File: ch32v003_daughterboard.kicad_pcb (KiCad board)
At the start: 2 copper layers, 39 x 45.2 mm, 7 parts, among them J1 Conn_02x05_Odd_Even, J2 Conn_01x03_Pin, P1 Header 7X2, P2 Header 7X2

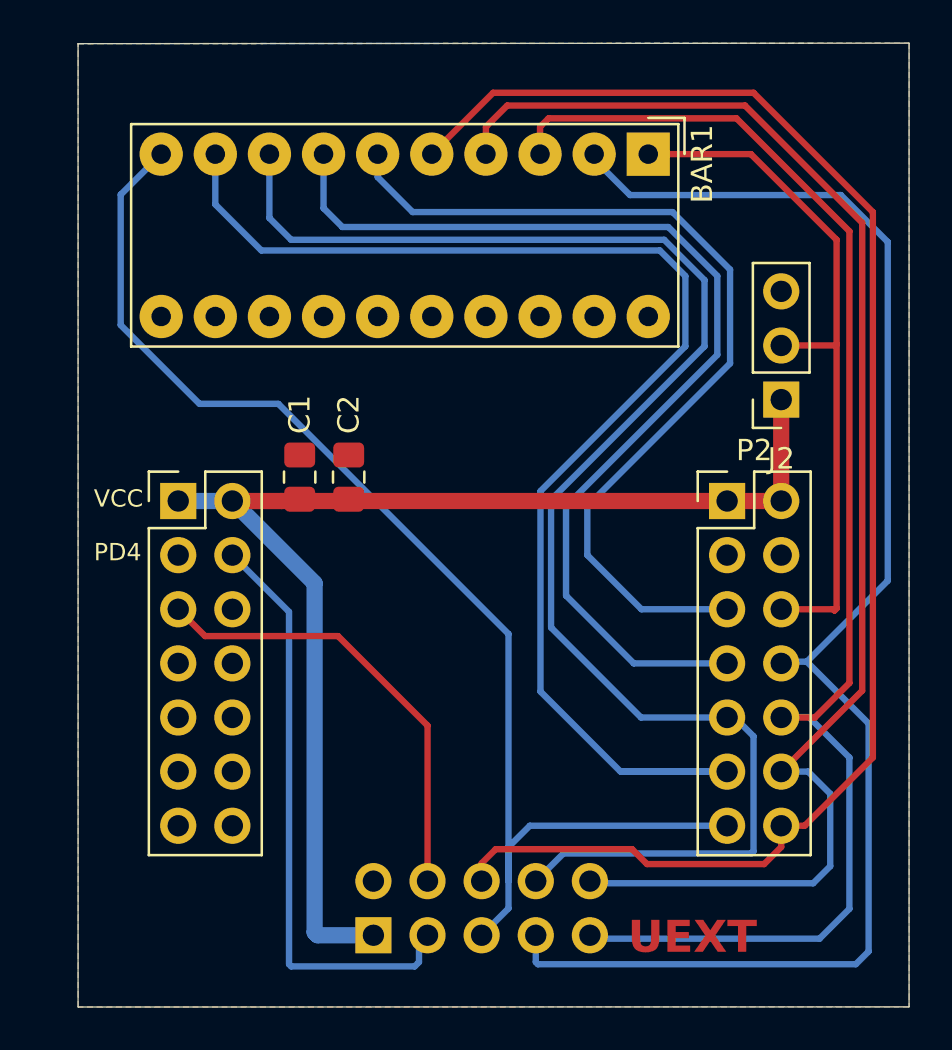
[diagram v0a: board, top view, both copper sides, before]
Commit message: free SDIO + pot.
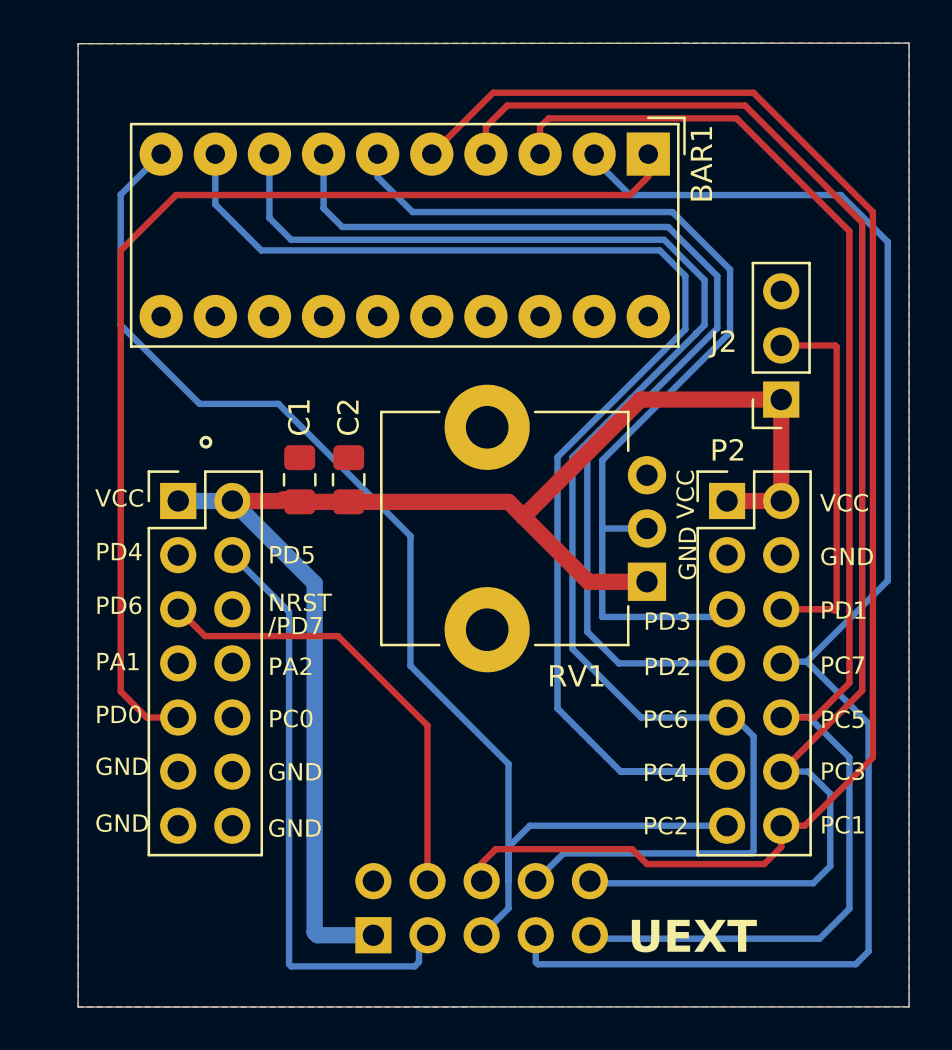
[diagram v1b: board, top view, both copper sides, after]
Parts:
- added RV1: Mouser PTN091-V05115K1B, Potentiometer_THT:Potentiometer_TT_P0915N, F.Cu at (155.7, 107.7)
- moved C1 0.12 mm to (139.4, 102.9)
- moved C2 0.12 mm to (141.7, 102.9)
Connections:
- BAR1 pad 1: /PD1 -> /PD0
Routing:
- net /PD0: track 0.00 -> 51.2 mm
- net /PD1: track 33.1 -> 17.6 mm
- net VCC: track 57.7 -> 69.8 mm
- net /PD3: track 43.2 -> 46.3 mm
- net /MOSI: track 71.7 -> 70.9 mm
- net /PC4: track 63.4 -> 62.7 mm
- net GND: vias 0 -> 1

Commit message: add FTDI RS232-USB
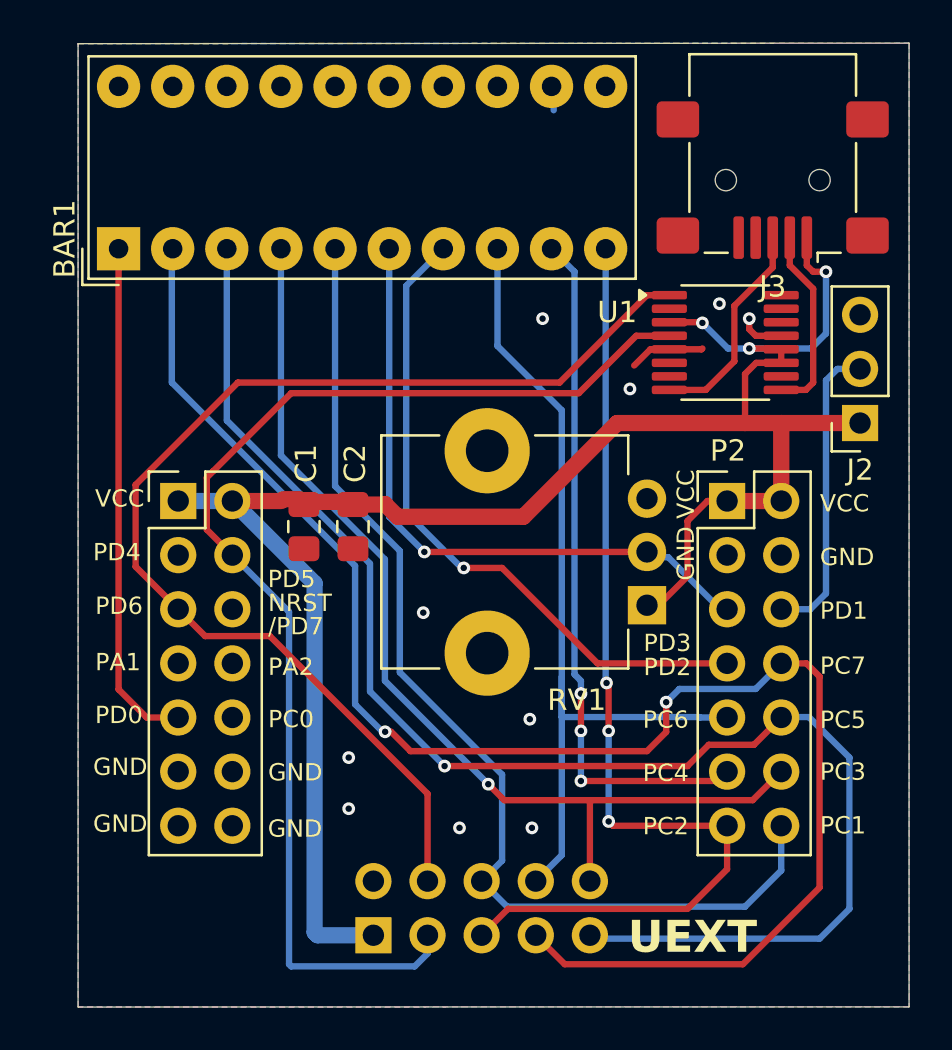
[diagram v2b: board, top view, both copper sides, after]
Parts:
- added J3: USB_B_Mini, Connector_USB:USB_Mini-B_Lumberg_2486_01_Horizontal, F.Cu at (161.6, 88.8)
- added U1: FT230XS, Package_SO:SSOP-16_3.9x4.9mm_P0.635mm, F.Cu at (159.4, 96.4)
- moved BAR1 25.3 mm to (130.9, 92.0), turned to 90 degrees
- moved J2 3.86 mm to (165.7, 100.2)
- moved C1 2.21 mm to (139.6, 105.1), turned to -90 degrees
- moved C2 2.21 mm to (141.9, 105.1), turned to -90 degrees
- moved RV1 1.10 mm to (155.7, 108.8)
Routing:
- net /PD6: track 21.3 -> 54.8 mm
- net /PC4: track 62.7 -> 32.6 mm, vias 0 -> 3
- net /MOSI: track 70.9 -> 41.1 mm
- net /PD5: track 28.0 -> 56.6 mm
- net /PD0: track 51.2 -> 24.0 mm
- net VCC: track 69.8 -> 91.8 mm, vias 0 -> 3
- net /PC1: track 72.2 -> 50.7 mm
- net /CS#: track 66.7 -> 47.6 mm, vias 0 -> 1
- net /PD2: track 48.7 -> 31.1 mm, vias 0 -> 1
- net /PD3: track 46.3 -> 30.7 mm, vias 0 -> 1
- net /PC2: track 59.9 -> 47.4 mm, vias 0 -> 3
- net Net-(J3-D+): track 0.00 -> 10.3 mm
- net Net-(J3-D-): track 0.00 -> 9.00 mm
- net GND: track 0.00 -> 6.78 mm, vias 1 -> 10
- net /MISO: track 69.9 -> 75.8 mm, vias 0 -> 2
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
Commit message: add push button
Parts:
- added R1: R, Resistor_SMD:R_0805_2012Metric_Pad1.20x1.40mm_HandSolder, F.Cu at (141.7, 101.0)
- added SW1: SW_SPST, Button_Switch_SMD:SW_SPST_B3SL-1002P, F.Cu at (135.9, 97.7)
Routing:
- net /PC0: track 0.00 -> 21.3 mm
- net VCC: track 91.8 -> 93.9 mm
- net /PD5: track 56.6 -> 57.9 mm
- net /PD6: track 54.8 -> 55.5 mm

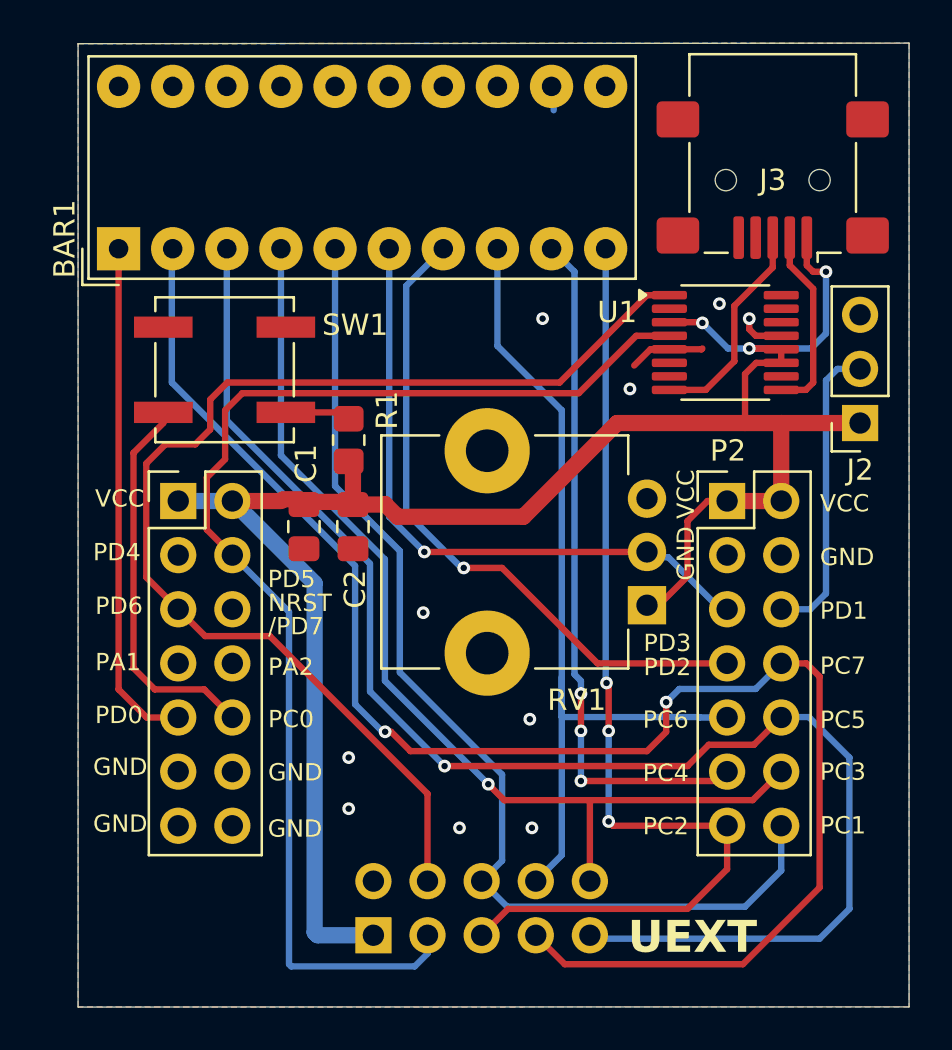
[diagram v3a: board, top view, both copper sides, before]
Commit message: add I2C pullup resistors
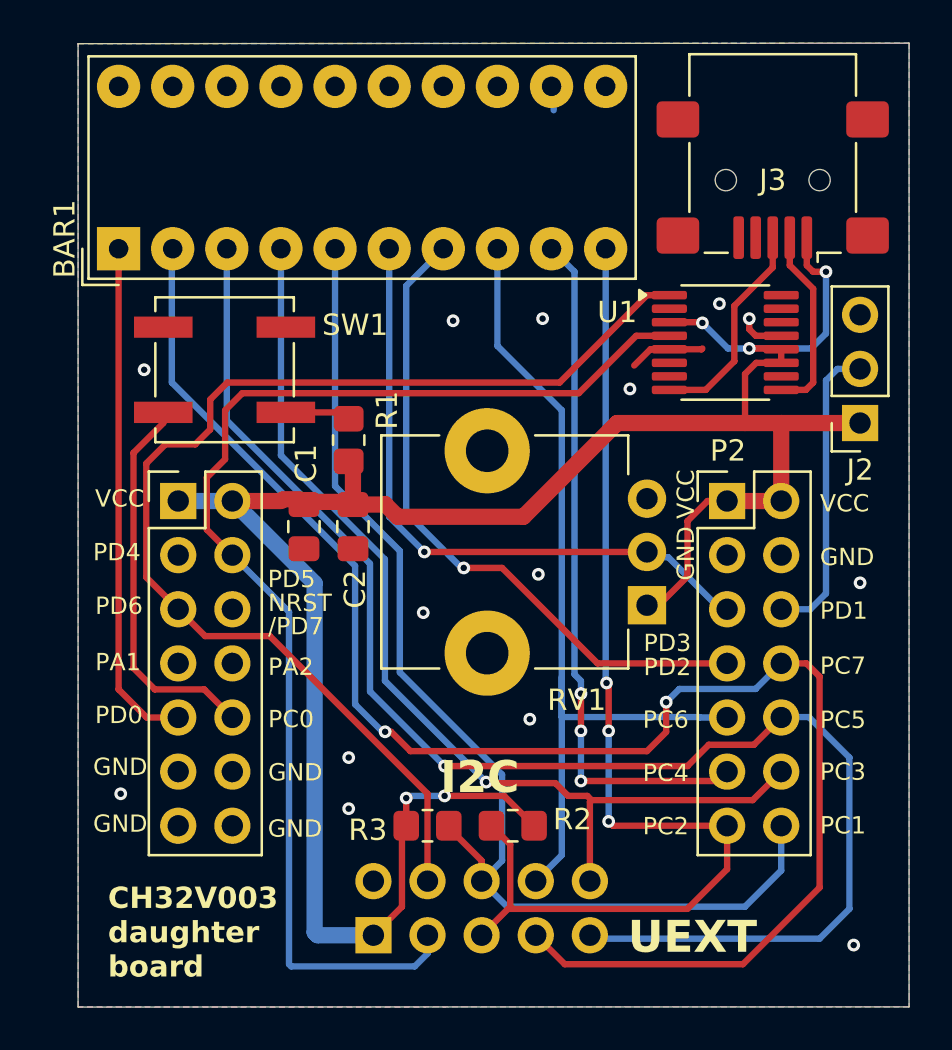
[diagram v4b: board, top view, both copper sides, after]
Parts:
- added R2: 5600, Resistor_SMD:R_0805_2012Metric_Pad1.20x1.40mm_HandSolder, F.Cu at (149.4, 119.1)
- added R3: 5600, Resistor_SMD:R_0805_2012Metric_Pad1.20x1.40mm_HandSolder, F.Cu at (145.4, 119.1)
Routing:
- net VCC: track 93.9 -> 107.6 mm, vias 3 -> 5
- net /PC2: track 47.4 -> 51.7 mm
- net /PC1: track 50.7 -> 53.9 mm
- net GND: vias 10 -> 14
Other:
- board text added: "CH32V003 daughter board"
- board text added: "I2C"

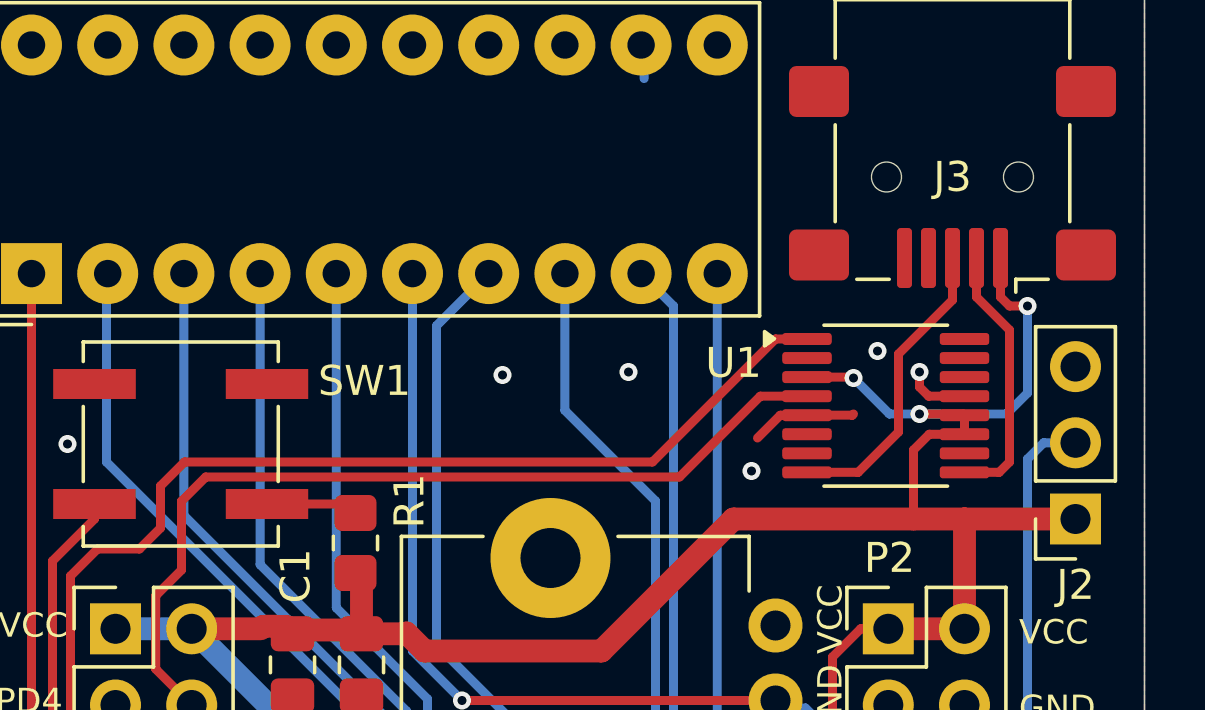
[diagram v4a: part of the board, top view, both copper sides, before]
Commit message: add missing passive and decoupling capacitors
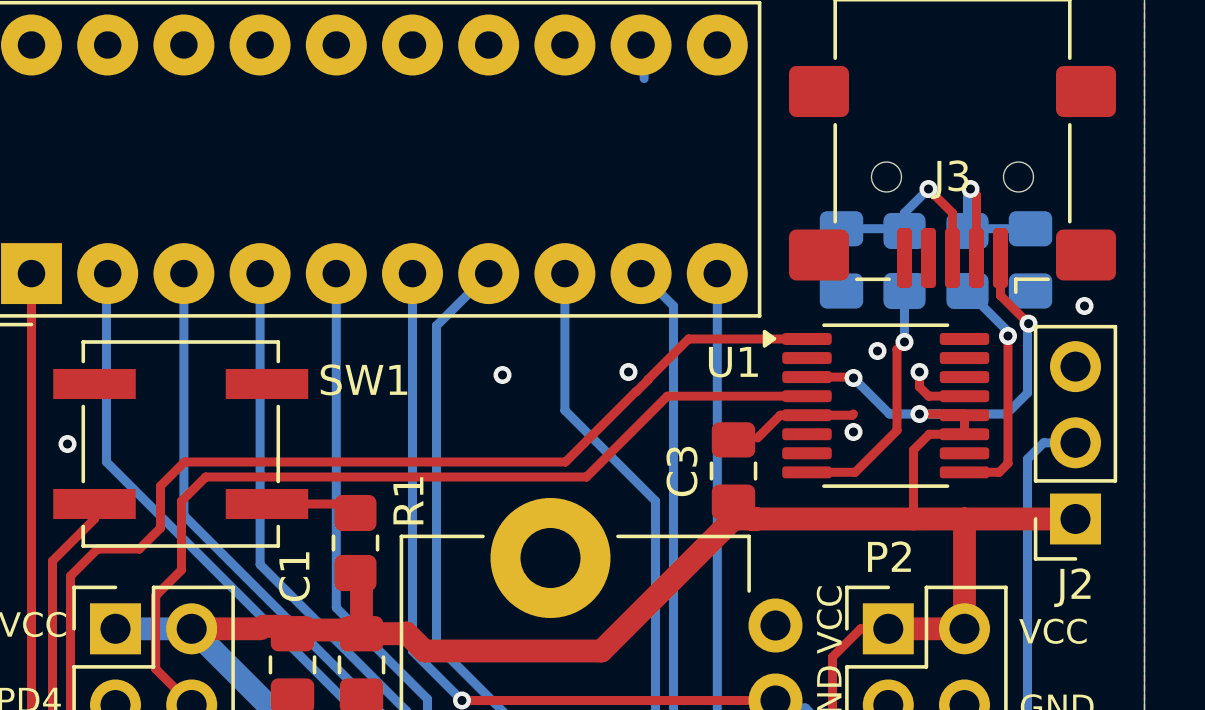
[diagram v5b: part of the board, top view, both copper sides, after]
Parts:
- added C3: 100n, Capacitor_SMD:C_0805_2012Metric_Pad1.18x1.45mm_HandSolder, F.Cu at (154.3, 98.6)
- added C4: 47p, Capacitor_SMD:C_0805_2012Metric_Pad1.18x1.45mm_HandSolder, B.Cu at (164.2, 91.6)
- added C5: 47p, Capacitor_SMD:C_0805_2012Metric_Pad1.18x1.45mm_HandSolder, B.Cu at (157.9, 91.6)
- added R4: 27, Resistor_SMD:R_0805_2012Metric_Pad1.20x1.40mm_HandSolder, B.Cu at (160.0, 91.6)
- added R5: 27, Resistor_SMD:R_0805_2012Metric_Pad1.20x1.40mm_HandSolder, B.Cu at (162.1, 91.6)
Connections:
- U1 pad 8: Net-(J3-D+) -> Net-(U1-USBDP)
- U1 pad 9: Net-(J3-D-) -> Net-(U1-USBDM)
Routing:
- net Net-(U1-USBDP): track 0.00 -> 8.33 mm, vias 0 -> 1
- net Net-(U1-USBDM): track 0.00 -> 7.88 mm, vias 0 -> 1
- net Net-(J3-D+): track 10.3 -> 6.49 mm, vias 0 -> 1
- net Net-(J3-D-): track 9.00 -> 5.96 mm, vias 0 -> 1
- net VCC: track 107.6 -> 108.3 mm
- net GND: vias 14 -> 15
